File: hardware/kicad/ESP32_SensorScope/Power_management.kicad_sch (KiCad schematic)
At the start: 30 parts, among them J7 Batt+, J8 Batt-, Q3 2N7002, SW1 Pwr switch, U13 AP3012, U14 AP63205WU

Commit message: something probobly
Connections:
- net Batt_sense renamed Batt_ADC
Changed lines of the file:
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@@
 	(text "VOUT=1.25*(1+R12/R18)=1.25*10.21=12,8V"
 		(exclude_from_sim no)
-		(at 85.598 92.71 0)
+		(at 69.342 92.964 0)
 		(effects
 			(font
@@
 		)
 	)
-	(global_label "Batt_sense"
+	(global_label "Batt_ADC"
 		(shape input)
 		(at 69.85 146.05 180)
@@
 		)
 		(property "Intersheetrefs" "${INTERSHEET_REFS}"
-			(at 56.6444 146.05 0)
+			(at 58.3982 146.05 0)
 			(effects
 				(font

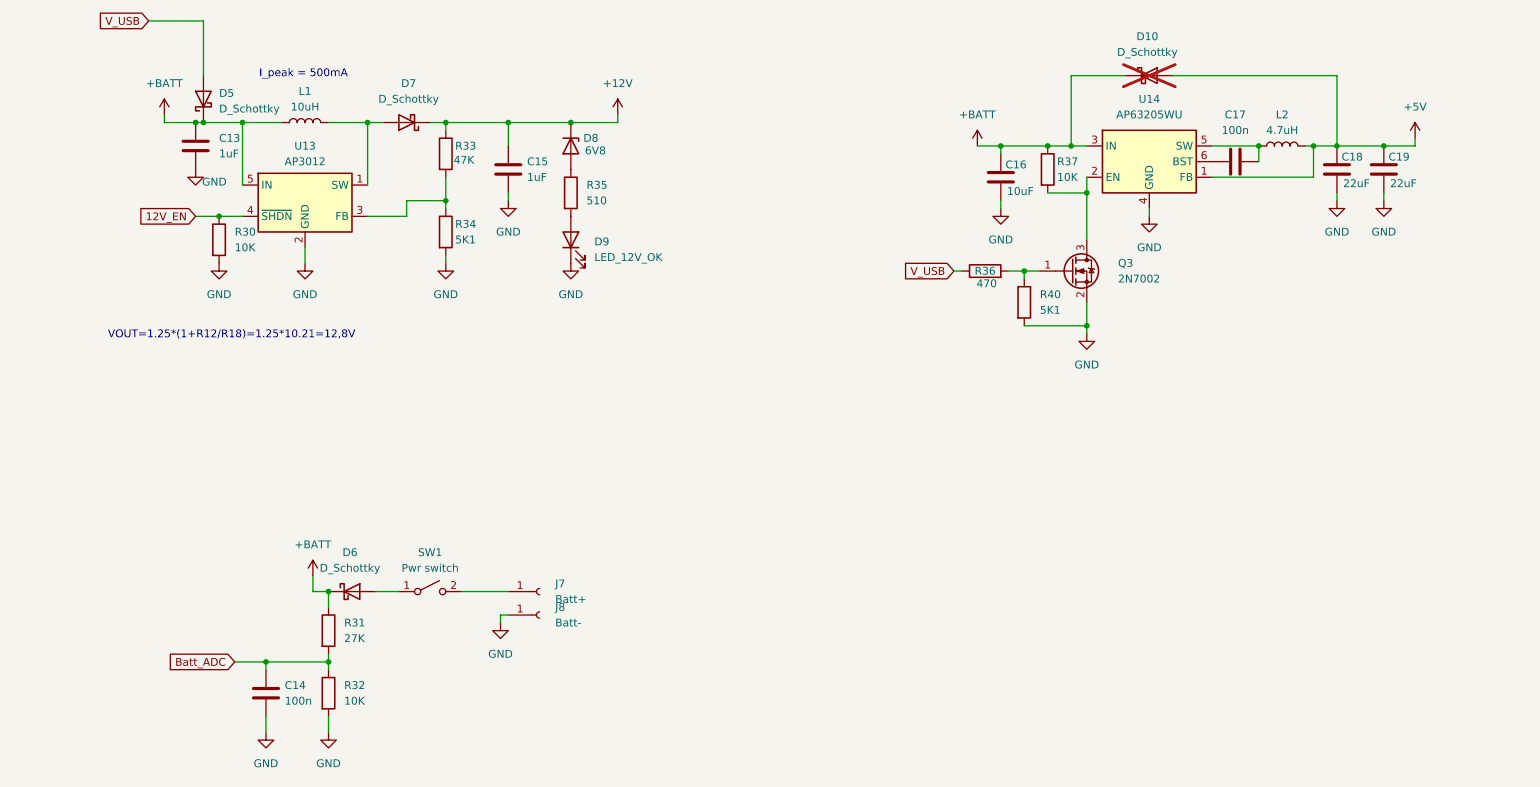
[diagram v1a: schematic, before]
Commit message: som updates on the schematics
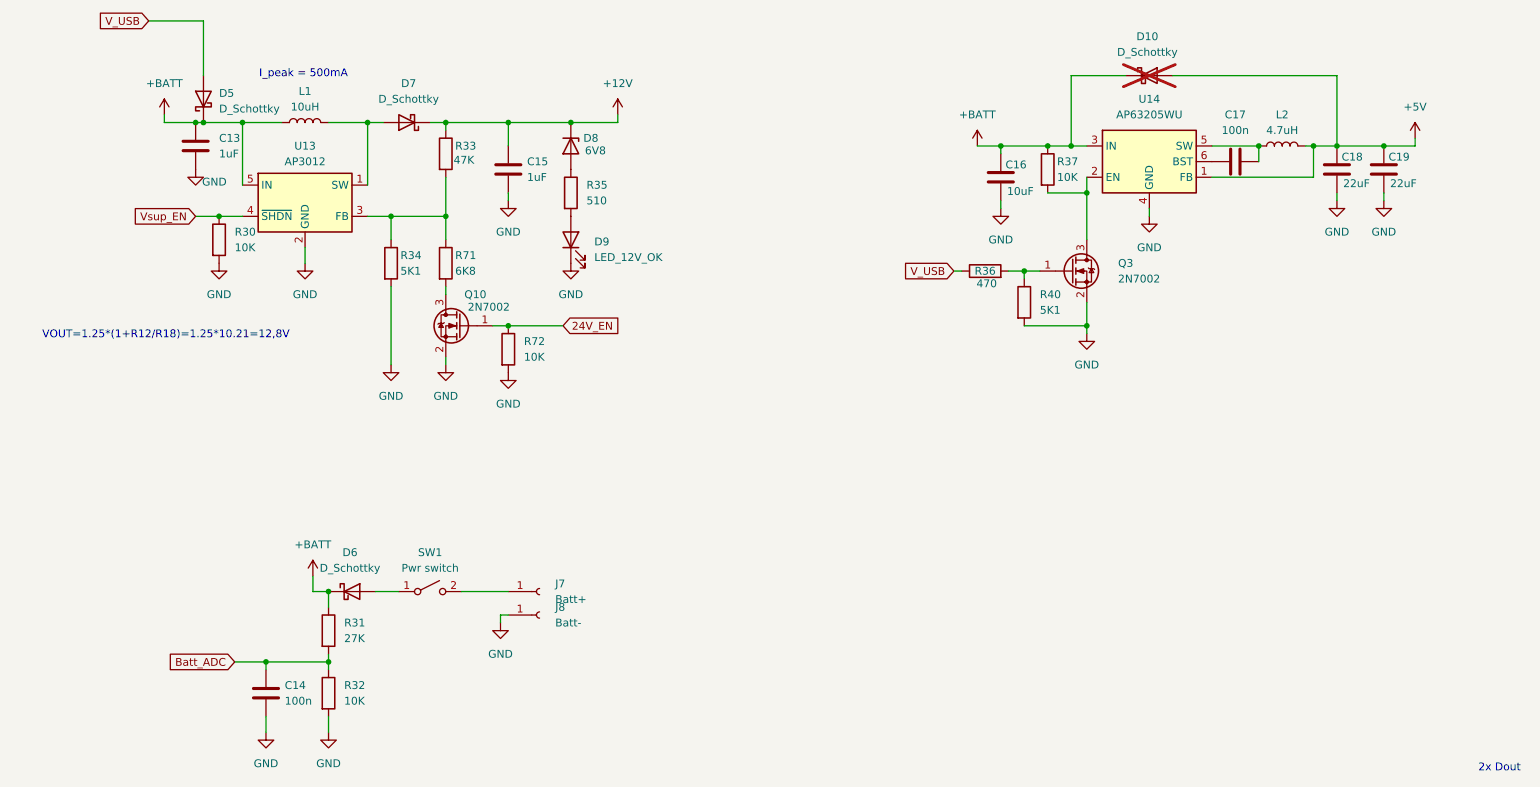
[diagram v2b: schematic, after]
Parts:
- added Q10: 2N7002, Package_TO_SOT_SMD:SOT-23, symbol Transistor_FET:2N7002
- added R71: 6K8, symbol Device:R
- added R72: 10K, symbol Device:R
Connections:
- net GND: now also Q10.2 (S), R72.2
- net at R33.2, R34.1, U13.3 (FB): now also R71.1
- net 12V_EN renamed Vsup_EN
- new net: Q10.3 (D), R71.2
- new net 24V_EN: Q10.1 (G), R72.1
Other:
- note added: "2x Dout"
- moved on the sheet: R34

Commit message: updatet schematic
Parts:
- removed D10: D_Schottky, symbol Device:D_Schottky
- added D12, D23: 6V8, symbol Device:D_Zener
- added Q11, Q12: 2N7002, Package_TO_SOT_SMD:SOT-23, symbol Transistor_FET:2N7002
- added R23: 47K, symbol Device:R
- R40: value 5K1 -> 10K
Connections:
- net +12V: now also R35.1; no longer D8.1 (K)
- net +5V: now also R23.1
- net 24V_EN: now also Q12.1 (G)
- net GND: now also D23.2 (A), Q11.2 (S), Q12.2 (S); no longer D9.1 (K)
- net at D8.2 (A): now also D12.1 (K), Q11.3 (D); no longer R35.1
- net Vsup_EN renamed Vout_EN
- new net: Q11.1 (G), Q12.3 (D), R23.2
- new net: D8.1 (K), D9.1 (K)
- new net: D12.2 (A), D23.1 (K)
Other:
- moved on the sheet: D8, D9, Q10, R34, R35, R71, R72

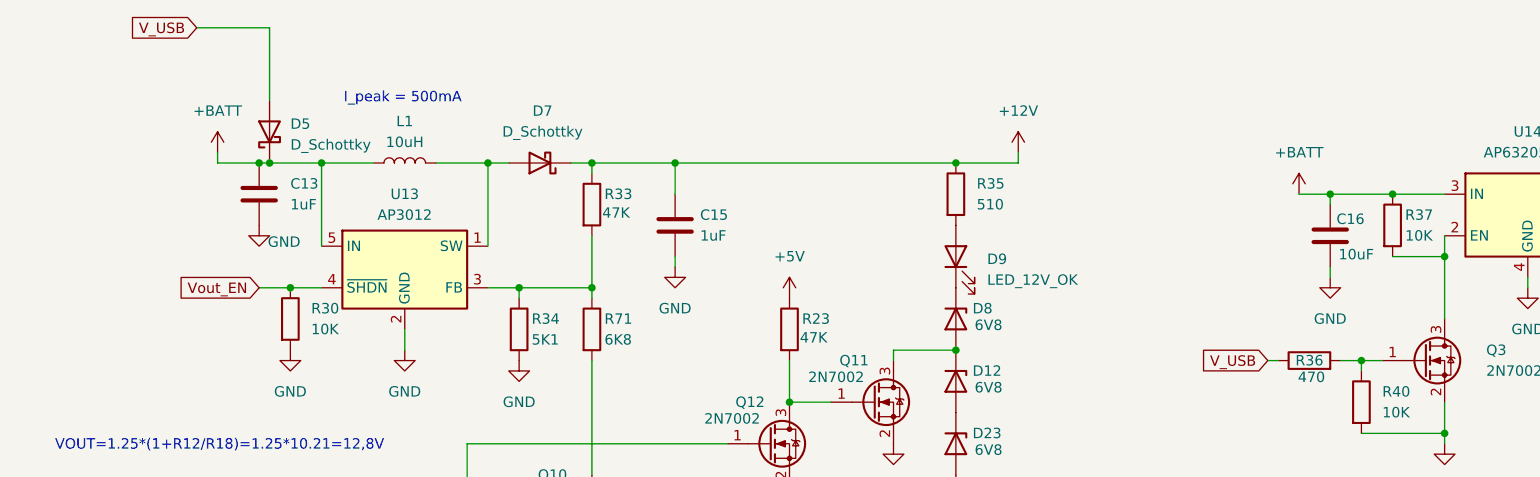
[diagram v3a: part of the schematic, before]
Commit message: addet some footprints"
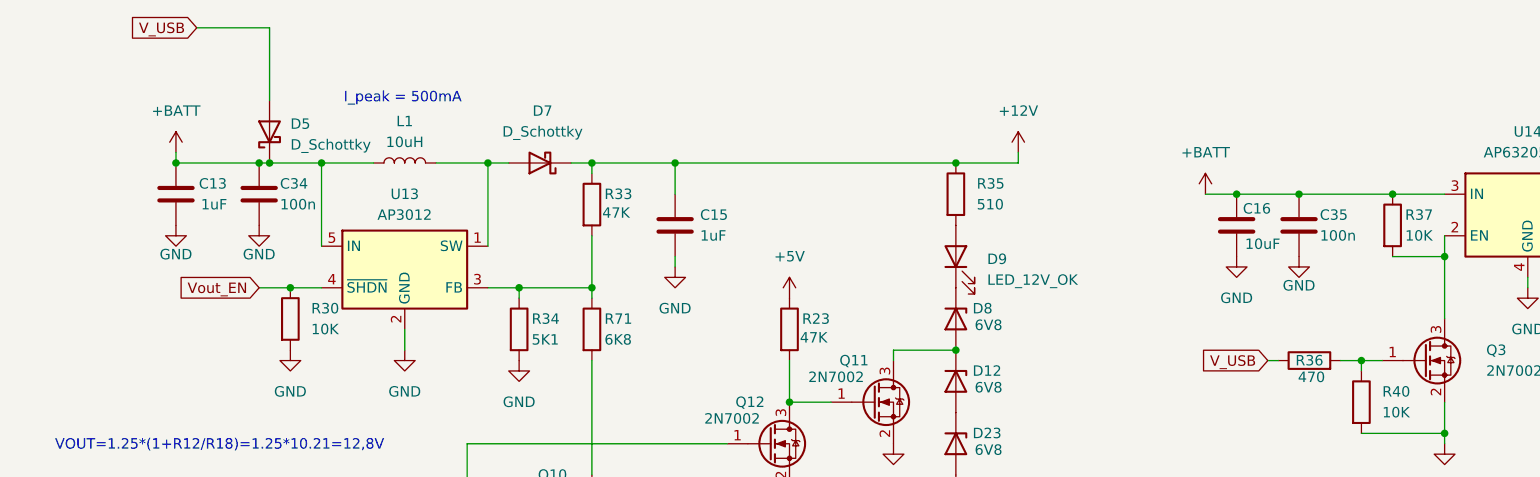
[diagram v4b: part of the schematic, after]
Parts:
- added C34, C35: 100n, Capacitor_SMD:C_0805_2012Metric, symbol Device:C
- C13, C14, C15, C17: footprint (none) -> Capacitor_SMD:C_0805_2012Metric
- C16, C18, C19: footprint (none) -> Capacitor_SMD:C_1206_3216Metric
- D5, D6: footprint (none) -> Diode_SMD:D_SMA
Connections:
- net +BATT: now also C34.1, C35.1
- net GND: now also C34.2, C35.2
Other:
- moved on the sheet: C13, C16
